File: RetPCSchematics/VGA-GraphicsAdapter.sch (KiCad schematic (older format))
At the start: 63 parts, among them J1 Bus_ISA_8bit, U1 74LS245, U10 74LVC1G18, U11 74LVC1G18, U12 74LVC1G18, U13 74LVC1G18, U14 74LVC1G18, U15 74LVC1G18, U16 74LVC1G18, U17 74LVC1G18, U18 74LVC1G18, U19 74LVC1G18, U2 628128, U20 74LVC1G18, U21 74LVC1G18, U22 74LVC1G18, U23 74LVC1G18, U24 74LS245, U25 74LS573, U26 74LS573, U27 74LS573, U28 TFP410, U29 4520, U3 74LVC1G18, U30 4520, U31 4520, U32 4520, U33 74LVC1G18, U34 74LVC1G18, U35 74LVC1G18, U36 74LVC1G18, U37 74LVC1G18, U38 74LVC1G18, U39 74LVC1G18, U4 74LVC2G157, U40 74LVC1G18, U41 74LVC1G18, U42 74LVC1G18, U43 74LVC1G18, U44 74LVC1G18, U45 74LVC1G18, U46 74LVC1G18, U47 74LVC1G18, U48 74LVC1G18, U49 74LVC1G18, U5 628128, U50 4520, U51 74LS573, U52 74LS573, U53 74LVC2G240, U55 74LS245, U56 74LS573, U57 74LS245, U58 ATmega644P-20PU, U6 4520, U7 74LS245, U8 SN74LVC245AN, U9 74LVC1G18, X1 DGOF5S3

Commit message: sync
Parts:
- added J?: 74320-9004, digikey-footprints:DVI_Female_74320-9004, symbol dk_USB-DVI-HDMI-Connectors:74320-9004
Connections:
- net labels added: (inv)LE
- net labels removed: LoadPulse
- wire segments 634 -> 666
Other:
- moved on the sheet: U28A, U?B

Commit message: Sync and start of rev 2.3
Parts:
- removed U13, U14, U15, U16, U17, U18, U19, U20, U21, U22, U23, U3: 74LVC1G18, symbol 74xGxx:74LVC1G18
- removed U25, U26, U27: 74LS573, symbol 74xx:74LS573
- removed U?: 74LS09, symbol 74xx:74LS09
- added U? (x12): 74LVC1G373, symbol 74xGxx:74LVC1G373
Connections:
- net labels removed: VideoDataPlexingUnit
- wire segments 666 -> 564
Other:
- moved on the sheet: J?, U28A, U?B

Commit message: sync and added different operation modes
Added full support for all different CGA modes and basicly finnished with schematics
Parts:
- removed U4: 74LVC2G157, symbol 74xGxx:74LVC2G157
- removed U53, U?: 74LVC2G240, symbol 74xGxx:74LVC2G240
- added U1, U2: 74LS21, Package_DIP:DIP-14_W7.62mm_Socket, symbol 74xx:74LS21
- added U11: 74AHC1G08, symbol 74xGxx:74AHC1G08
- added U12: 74LVC2G240, symbol 74xGxx:74LVC2G240
- added U15: 4520, symbol 4xxx:4520
- added U4: 74AUC1G18, RetPC:SOIC-16-6.4, symbol 74xGxx:74AUC1G18
- added U5: 74AUC1G18, symbol 74xGxx:74AUC1G18
- U10: renamed from U32; footprint (none) -> Package_SO:SOP-16_4.4x10.4mm_P1.27mm
- U3: renamed from U1; footprint (none) -> Package_DIP:DIP-20_W7.62mm_Socket
- U6: footprint (none) -> Package_SO:SOP-16_4.4x10.4mm_P1.27mm
- U7: renamed from U29; footprint (none) -> Package_SO:SOP-16_4.4x10.4mm_P1.27mm
- U8: renamed from U30; footprint (none) -> Package_SO:SOP-16_4.4x10.4mm_P1.27mm
- U9: renamed from U31; footprint (none) -> Package_SO:SOP-16_4.4x10.4mm_P1.27mm
- gave numbers to parts that had none: 15
- renumbered U51 to U13, U55 to U14, U33 to U16, U34 to U17, U35 to U18, U36 to U19, U37 to U20, U38 to U21, U39 to U22, U40 to U23, U41 to U24, U42 to U25, U43 to U26, U44 to U27, U45 to U28, U46 to U29, U47 to U30, U48 to U31, U49 to U32, U56 to U33, U57 to U34, U52 to U35, U58 to U36, U5 to U37, U2 to U38, U50 to U39, U7 to U40, U8 to U41, U9 to U42, U10 to U43, U11 to U44, U12 to U45, U24 to U58, U28 to U60
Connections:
- net labels added: CS, CS(inv), IOW, OP1, OP2
- net labels removed: BusRead
- wire segments 564 -> 612
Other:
- note added: "^ Actually a mux:s but didn't have good symbol\n"

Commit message: Removed unnesescary muxes, Added CPLD symbol
Fixed som layout, added Atmel CPLD and CPLD symbol
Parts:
- removed U13: 74LS573, symbol 74xx:74LS573
- removed U14, U34: 74LS245, symbol 74xx:74LS245
- removed U16, U17, U18, U19, U20, U21, U22, U23, U24, U25, U26, U27, U28, U29, U30, U31, U32: 74LVC1G18, symbol 74xGxx:74LVC1G18
- removed U3: 74LS245, Package_DIP:DIP-20_W7.62mm_Socket, symbol 74xx:74LS245
- added U? (x2): 74LS245, symbol 74xx:74LS245
- added U? (x2): 74AUC2G125, symbol 74xGxx:74AUC2G125
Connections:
- net labels removed: A18, A19
- wire segments 612 -> 516
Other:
- moved on the sheet: U12A, U4, U5

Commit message: Changed to Rev 3.0 CPLD version
Swapped lots of discrete logic with CPLDs
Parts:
- removed U1, U2: 74LS21, Package_DIP:DIP-14_W7.62mm_Socket, symbol 74xx:74LS21
- removed U10, U6, U7, U8, U9: 4520, Package_SO:SOP-16_4.4x10.4mm_P1.27mm, symbol 4xxx:4520
- removed U11: 74AHC1G08, symbol 74xGxx:74AHC1G08
- removed U15, U39: 4520, symbol 4xxx:4520
- removed U4: 74AUC1G18, RetPC:SOIC-16-6.4, symbol 74xGxx:74AUC1G18
- removed U5: 74AUC1G18, symbol 74xGxx:74AUC1G18
- added R? (x7): 4.7k, symbol Device:R
- added U? (x5): ATF22V10D, MODULE, symbol ATF22V10D:ATF22V10D
- added U? (x2): 74LVC2G240, symbol 74xGxx:74LVC2G240
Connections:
- net labels added: DE, GEnd, Hsync, OP, Sel, Vsync
- net labels removed: OP1, OP2
- wire segments 516 -> 490
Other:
- note removed: "^ Actually a mux:s but didn't have good symbol\n"
- moved on the sheet: J1, J2, U12A, U12B, U36, U37, U38, U40, U41, U42, U43, U44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

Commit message: Finalised schematic and started routing
Final schematic, assigned footprints and started routing
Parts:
- removed U33, U35: 74LS573, symbol 74xx:74LS573
- removed U59: 74LS09, symbol 74xx:74LS09
- added U15: 74LVC2G240, Package_SO:VSSOP-8_2.3x2mm_P0.5mm, symbol 74xGxx:74LVC2G240
- added U7, U9: 74LS245, Package_DIP:DIP-20_W7.62mm_Socket, symbol 74xx:74LS245
- R1: renamed from R?; footprint (none) -> Resistor_THT:R_Axial_DIN0411_L9.9mm_D3.6mm_P5.08mm_Vertical
- R2, R3, R4, R5, R6, R7: renamed from R?; footprint (none) -> Resistor_THT:R_Axial_DIN0411_L9.9mm_D3.6mm_P7.62mm_Vertical
- U1, U16, U2: renamed from U?; footprint (none) -> Package_SO:VSSOP-8_2.3x2mm_P0.5mm
- U11: renamed from U37; footprint (none) -> Package_DIP:DIP-24_W7.62mm_Socket
- U12: renamed from U38; footprint (none) -> Package_DIP:DIP-24_W7.62mm_Socket
- U14: renamed from U40; footprint (none) -> Package_DIP:DIP-20_W7.62mm_Socket
- U16, U2: renamed from U12; footprint (none) -> Package_SO:VSSOP-8_2.3x2mm_P0.5mm
- U17: renamed from U42; footprint (none) -> Package_TO_SOT_SMD:SOT-23-6_Handsoldering
- U18: renamed from U43; footprint (none) -> Package_TO_SOT_SMD:SOT-23-6_Handsoldering
- U19: renamed from U44; footprint (none) -> Package_TO_SOT_SMD:SOT-23-6_Handsoldering
- U20: renamed from U45; footprint (none) -> Package_TO_SOT_SMD:SOT-23-6_Handsoldering
- U21, U3, U37, U4, U6: renamed from U?; footprint MODULE -> Package_DIP:DIP-24_W7.62mm_Socket
- U22: renamed from U58; footprint (none) -> Package_DIP:DIP-22_W7.62mm_Socket
- U23: renamed from U46; footprint (none) -> Package_TO_SOT_SMD:SOT-23-6_Handsoldering
- U24: renamed from U47; footprint (none) -> Package_TO_SOT_SMD:SOT-23-6_Handsoldering
- U25: renamed from U48; footprint (none) -> Package_TO_SOT_SMD:SOT-23-6_Handsoldering
- U26: renamed from U49; footprint (none) -> Package_TO_SOT_SMD:SOT-23-6_Handsoldering
- U27: renamed from U50; footprint (none) -> Package_TO_SOT_SMD:SOT-23-6_Handsoldering
- U28: renamed from U51; footprint (none) -> Package_TO_SOT_SMD:SOT-23-6_Handsoldering
- U29: renamed from U52; footprint (none) -> Package_TO_SOT_SMD:SOT-23-6_Handsoldering
- U30: renamed from U53; footprint (none) -> Package_TO_SOT_SMD:SOT-23-6_Handsoldering
- U31: renamed from U54; footprint (none) -> Package_TO_SOT_SMD:SOT-23-6_Handsoldering
- U32: renamed from U55; footprint (none) -> Package_TO_SOT_SMD:SOT-23-6_Handsoldering
- U33: renamed from U56; footprint (none) -> Package_TO_SOT_SMD:SOT-23-6_Handsoldering
- U34: renamed from U57; footprint (none) -> Package_TO_SOT_SMD:SOT-23-6_Handsoldering
- U5, U8: renamed from U?; footprint (none) -> Package_DIP:DIP-20_W7.62mm_Socket
- renumbered U36 to U10, U41 to U13, U60 to U36, U61 to U36
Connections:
- net labels added: ALEN(inv), DR, REG, RST, RST(inv)
- wire segments 490 -> 540

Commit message: sync
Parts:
- removed R1: 4.7k, Resistor_THT:R_Axial_DIN0411_L9.9mm_D3.6mm_P5.08mm_Vertical, symbol Device:R
- removed R2, R3, R4, R5, R6, R7: 4.7k, Resistor_THT:R_Axial_DIN0411_L9.9mm_D3.6mm_P7.62mm_Vertical, symbol Device:R
- added RN1: R_Network08, Resistor_THT:R_Array_SIP9, symbol Device:R_Network08
- U11, U12: footprint Package_DIP:DIP-24_W7.62mm_Socket -> SMD_Packages:SOJ-32
- U21, U3, U4, U6: symbol ATF22V10D:ATF22V10D -> VGA-GraphicsAdapter-rescue:ATF22V10D-ATF22V10D
- U36: footprint (none) -> retsmd:HQFP-64_10x10mm_Pitch0.5mm_handsoldering
- U37: value ATF22V10D -> ATF750C; symbol ATF22V10D:ATF22V10D -> VGA-GraphicsAdapter-rescue:ATF22V10D-ATF22V10D
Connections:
- wire segments 540 -> 549

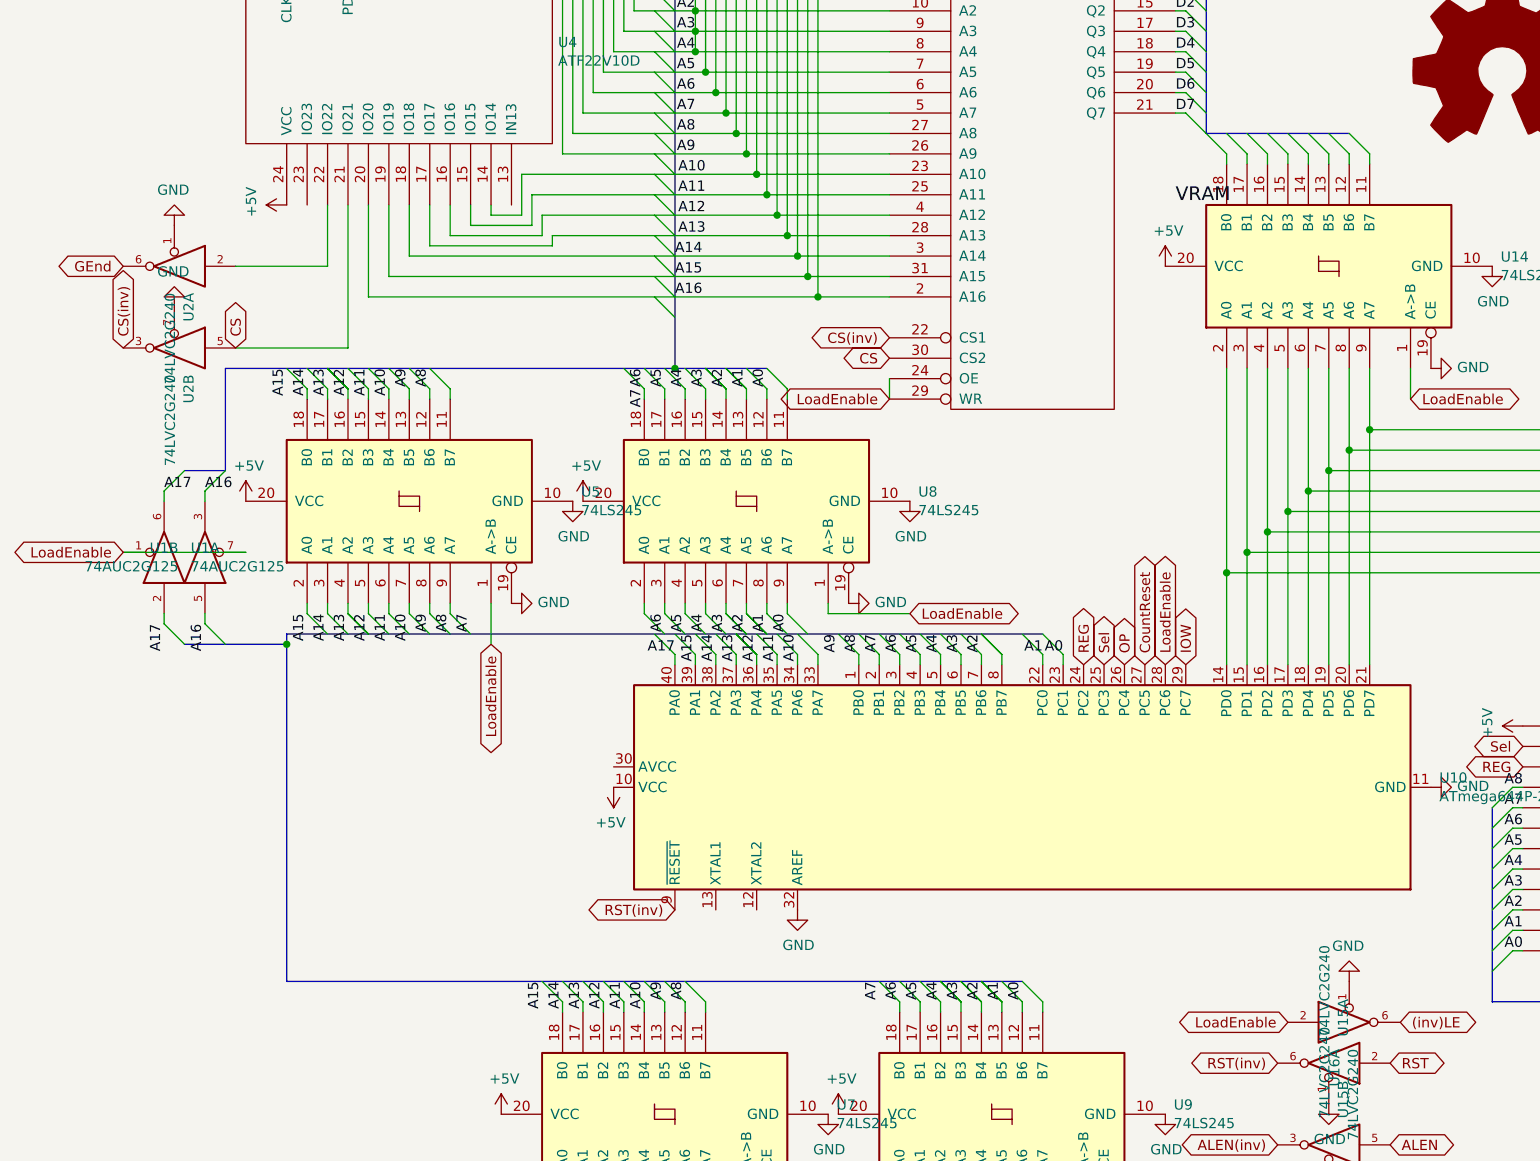
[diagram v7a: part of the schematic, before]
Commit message: Routed 2/3 of adapter and sync
sync and routed circuit a bit more
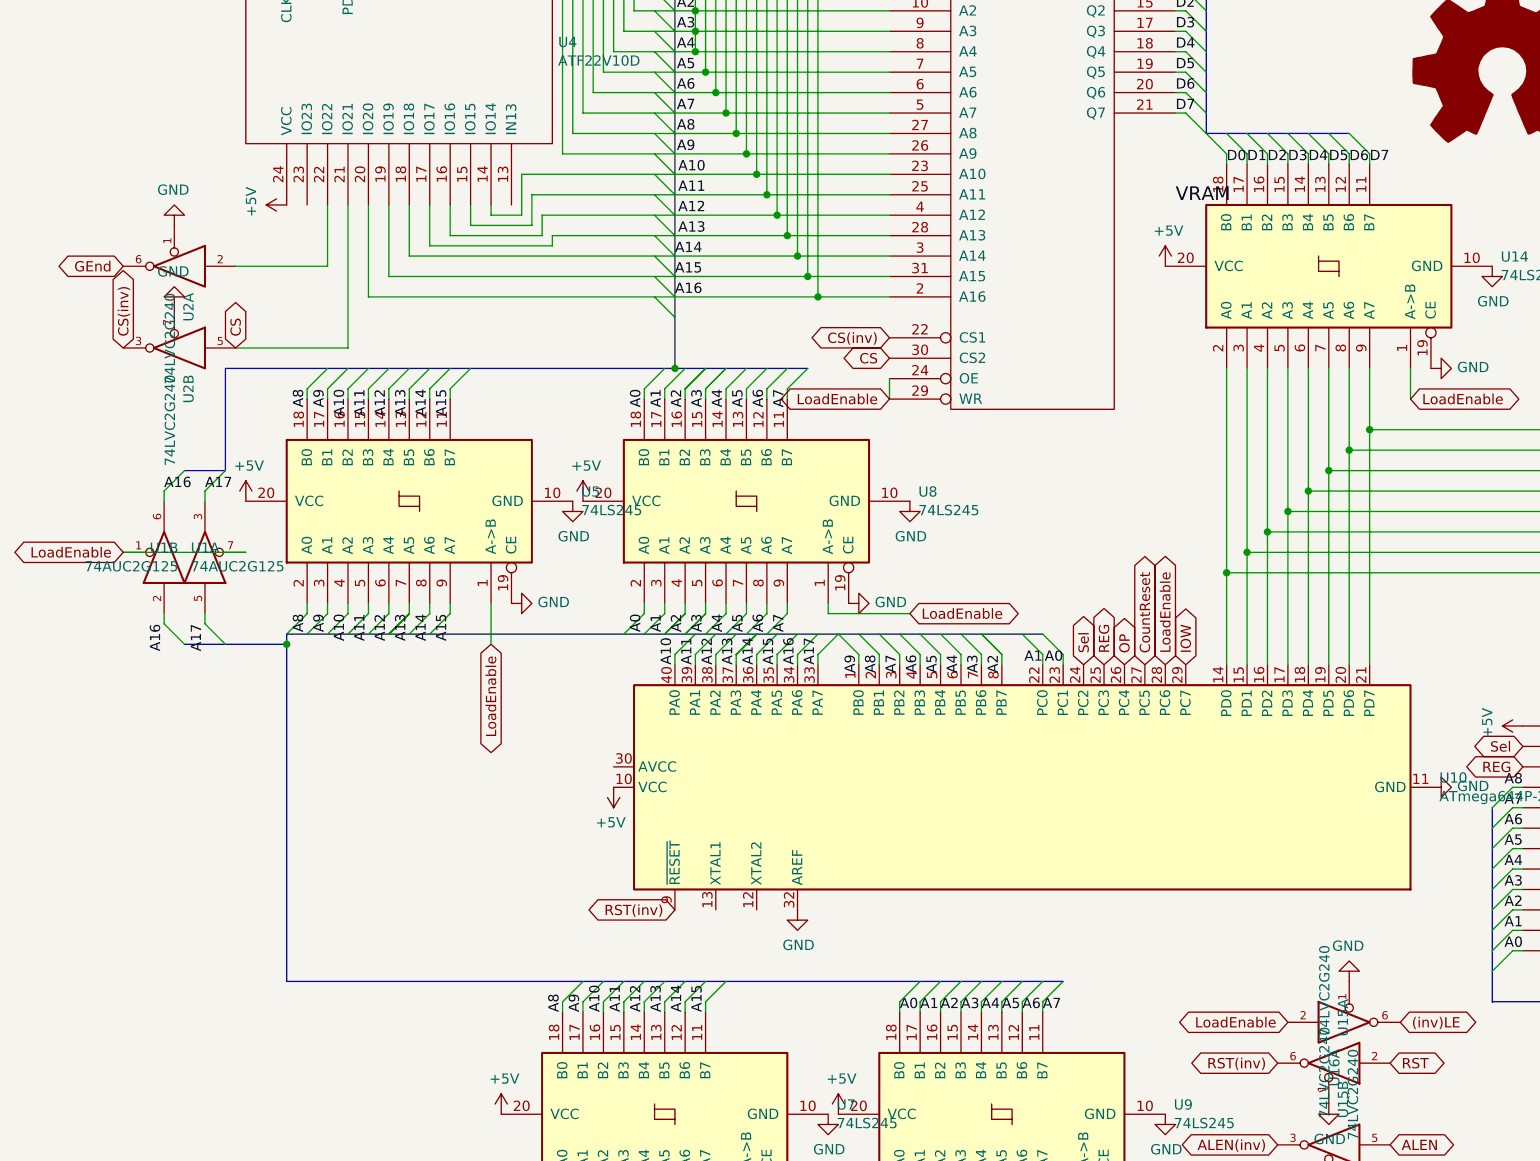
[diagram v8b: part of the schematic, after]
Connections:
- net A0: now also U10.6 (PB5), U10.7 (PB6), U10.8 (PB7), U8.14 (B4), U8.15 (B3), U8.16 (B2), U8.17 (B1), U8.18 (B0), U8.2 (A0), U8.3 (A1), U8.4 (A2), U9.14 (B4), U9.15 (B3), U9.16 (B2), U9.17 (B1), U9.18 (B0); no longer U8.7 (A5), U8.8 (A6), U8.9 (A7)
- net A10: now also U10.40 (PA0), U5.16 (B2), U5.4 (A2), U7.16 (B2); no longer U5.7 (A5)
- net A11: now also U10.39 (PA1), U5.15 (B3), U5.5 (A3), U7.15 (B3); no longer U5.6 (A4)
- net A12: now also U10.38 (PA2), U5.14 (B4), U5.6 (A4), U7.14 (B4); no longer U5.5 (A3)
- net A13: now also U10.37 (PA3), U5.13 (B5), U5.7 (A5), U7.13 (B5); no longer U5.4 (A2)
- net A14: now also U10.36 (PA4), U5.12 (B6), U5.8 (A6), U7.12 (B6); no longer U5.3 (A1)
- net A15: now also U10.35 (PA5), U5.11 (B7), U5.9 (A7), U7.11 (B7); no longer U5.2 (A0)
- net A16: now also U1.2, U1.6, U10.34 (PA6); no longer U1.3, U1.5
- net A17: now also U1.3, U1.5, U10.33 (PA7); no longer U1.2, U1.6, U10.40 (PA0)
- net A5: now also U10.5 (PB4), U8.13 (B5), U8.7 (A5), U9.13 (B5); no longer U8.4 (A2)
- net A6: now also U10.4 (PB3), U8.12 (B6), U8.8 (A6), U9.12 (B6); no longer U8.3 (A1)
- net A7: now also U10.3 (PB2), U8.11 (B7), U8.9 (A7), U9.11 (B7); no longer U8.18 (B0)
- net A8: now also U10.2 (PB1), U5.18 (B0), U5.2 (A0), U7.18 (B0); no longer U5.9 (A7)
- net A9: now also U10.1 (PB0), U5.17 (B1), U5.3 (A1), U7.17 (B1); no longer U5.8 (A6)
- net D0: now also U14.18 (B0)
- net D1: now also U14.17 (B1)
- net D2: now also U14.16 (B2)
- net D3: now also U14.15 (B3)
- net D4: now also U14.14 (B4)
- net D5: now also U14.13 (B5)
- net D6: now also U14.12 (B6)
- net D7: now also U14.11 (B7)
- net REG: now also U10.25 (PC3); no longer U10.24 (PC2)
- net Sel: now also U10.24 (PC2); no longer U10.25 (PC3)
